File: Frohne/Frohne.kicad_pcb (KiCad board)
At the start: 4 copper layers, 100 x 100 mm, 215 parts, among them J1 ADC IN, J10 Conn_01x20_Socket, J11 SDR ANT, J12 SDR Out, J2 Conn_02x20_Counter_Clockwise, J3 Conn_02x20_Counter_Clockwise, J4 Conn_01x20_Socket, J5 Conn_01x02, J7 Conn_01x01_Pin, J8 BNC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

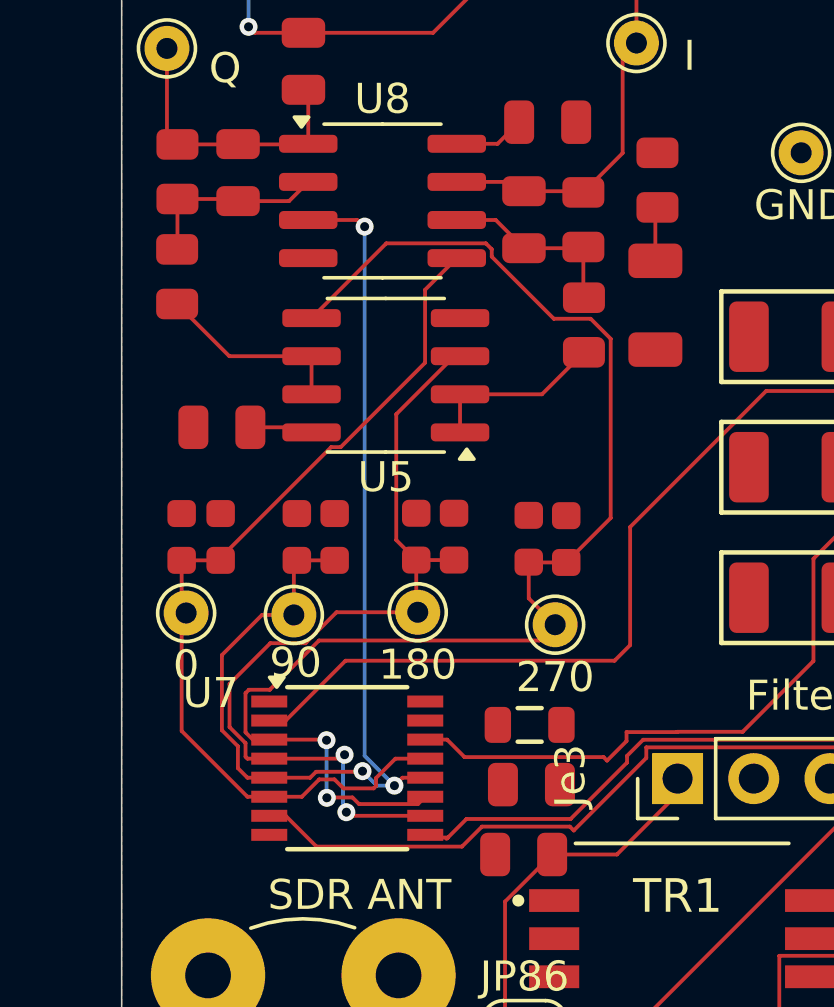
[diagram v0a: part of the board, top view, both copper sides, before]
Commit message: Made length of sampling caps the same.
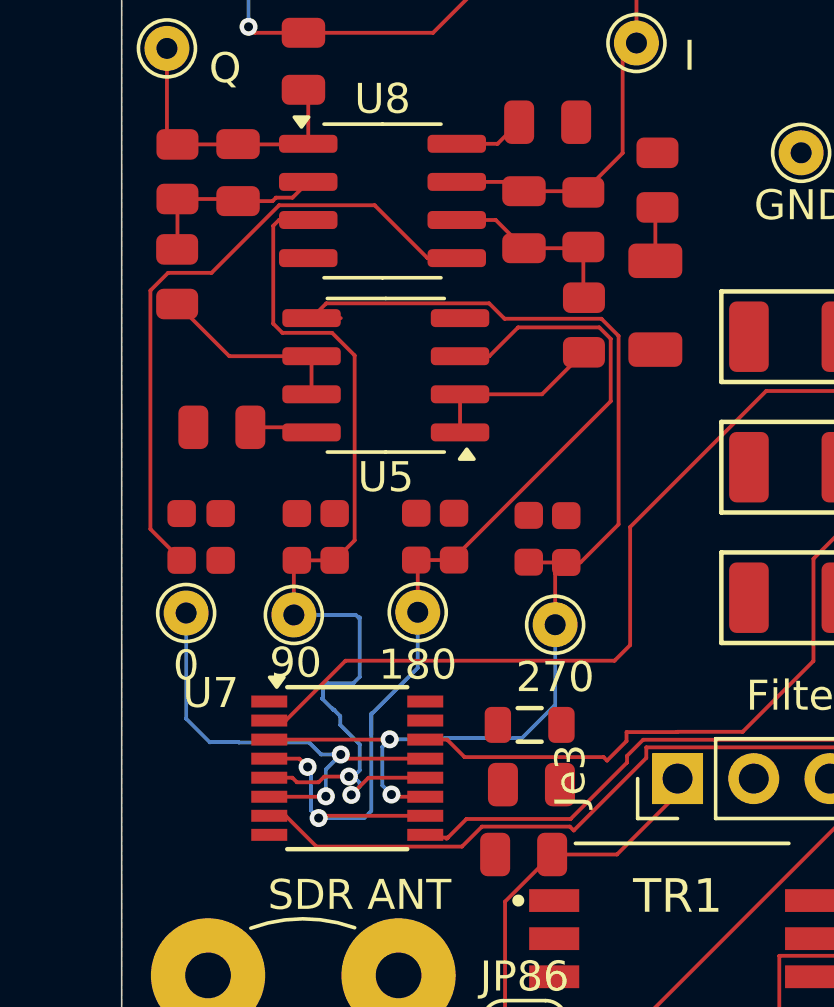
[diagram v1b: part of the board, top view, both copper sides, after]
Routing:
- net Net-(U7-1B1): track 30.5 -> 37.1 mm, vias 0 -> 2
- net Net-(U5A-+): track 29.0 -> 34.8 mm
- net Net-(U5B-+): track 45.0 -> 39.8 mm
- net Net-(U7-1B2): track 37.9 -> 33.6 mm, vias 3 -> 2
